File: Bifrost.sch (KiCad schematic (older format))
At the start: 28 parts, among them IC1 DS1085Z-10+, IC2 DS1085Z-10+, J1 OIP, J10 Barrel_Jack_Switch, J5 CalCK

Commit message: Added soldering options
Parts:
- added R10, R13, R14, R17, R18, R19, R3, R4, R5, R6, R9: 0, Resistor_SMD:R_0603_1608Metric_Pad0.98x0.95mm_HandSolder, symbol Device:R
- gave numbers to parts that had none: 4
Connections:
- wire segments 118 -> 145
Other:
- moved on the sheet: IC1, IC2, IOH1, J1, J10, J5, R1, R2, R49, R52, R53, R56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

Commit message: Added Logic gate buffer for the oscillator
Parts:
- removed U3, U4: BPF-E16, LibPersoNadj:Mini-Circuits_HR1176, symbol LibPersoNadj:BPF-E16
- added U5, U6: 74AHC1G04, Package_TO_SOT_SMD:SOT-353_SC-70-5, symbol 74xGxx:74AHC1G04
- RV1, RV2: footprint (none) -> Potentiometer_THT:Potentiometer_Bourns_3266Y_Vertical
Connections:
- net labels added: VDD
- wire segments 145 -> 147
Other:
- moved on the sheet: IC1, IC2, POWER1, R100, R71, R72

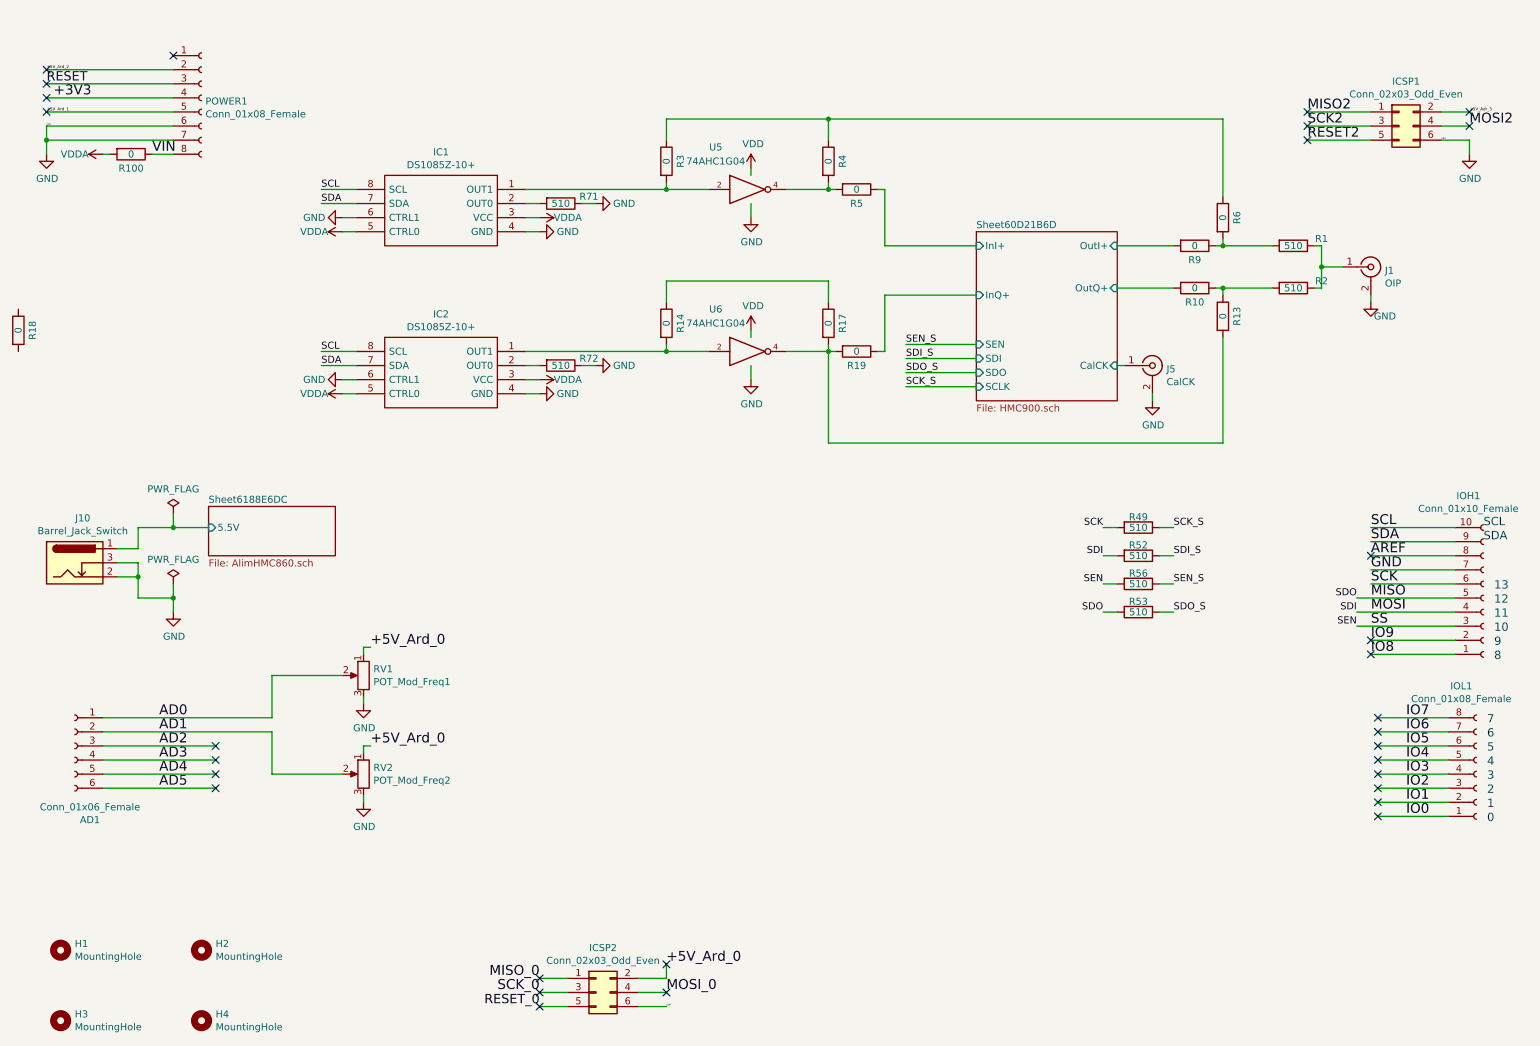
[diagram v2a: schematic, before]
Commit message: Added filtering capa and rearanged analogue in (A1=>A4)
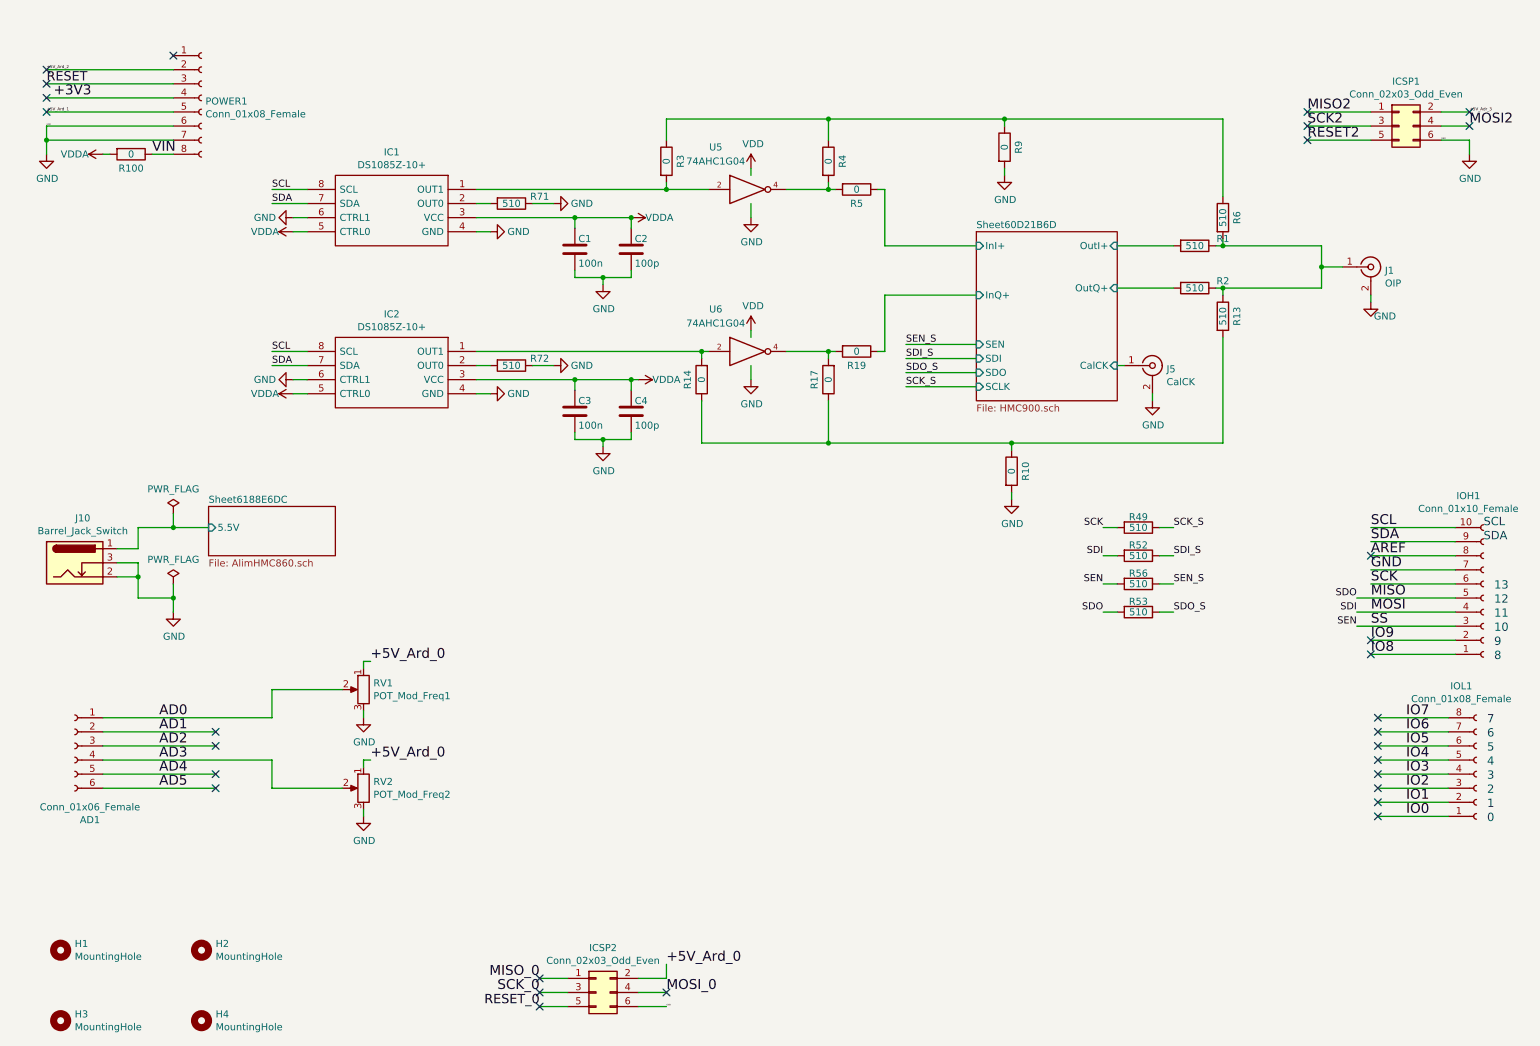
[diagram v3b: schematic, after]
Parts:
- removed R18: 0, Resistor_SMD:R_0603_1608Metric_Pad0.98x0.95mm_HandSolder, symbol Device:R
- added C1, C3: 100n, Capacitor_SMD:C_0603_1608Metric_Pad1.08x0.95mm_HandSolder, symbol Device:C
- added C2, C4: 100p, Capacitor_SMD:C_0603_1608Metric_Pad1.08x0.95mm_HandSolder, symbol Device:C
- R13, R6: value 0 -> 510
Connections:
- net AD1: no longer RV2.2
- net AD3: now also RV2.2
- net GND: now also R10.2, R9.2, C1.1, C2.1, C3.1, C4.1
- net Sheet60D21B6D/OutI+: now also R1.2; no longer R9.2
- net Sheet60D21B6D/OutQ+: now also R2.2; no longer R10.2
- net VDDA: now also C1.2, C2.2, C3.2, C4.2
- net at J1.1 (In), R1.1, R2.1: now also R13.1, R6.2
- net at R17.2, R19.2, U6.4: no longer R13.2
- net at R3.1, R4.1, R6.1: now also R9.1
- net at R14.1, R17.1: now also R10.1, R13.2
- no-connect marks 30 -> 29
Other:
- moved on the sheet: IC1, IC2, R1, R14, R17, R2, R71, R72, RV1, RV2

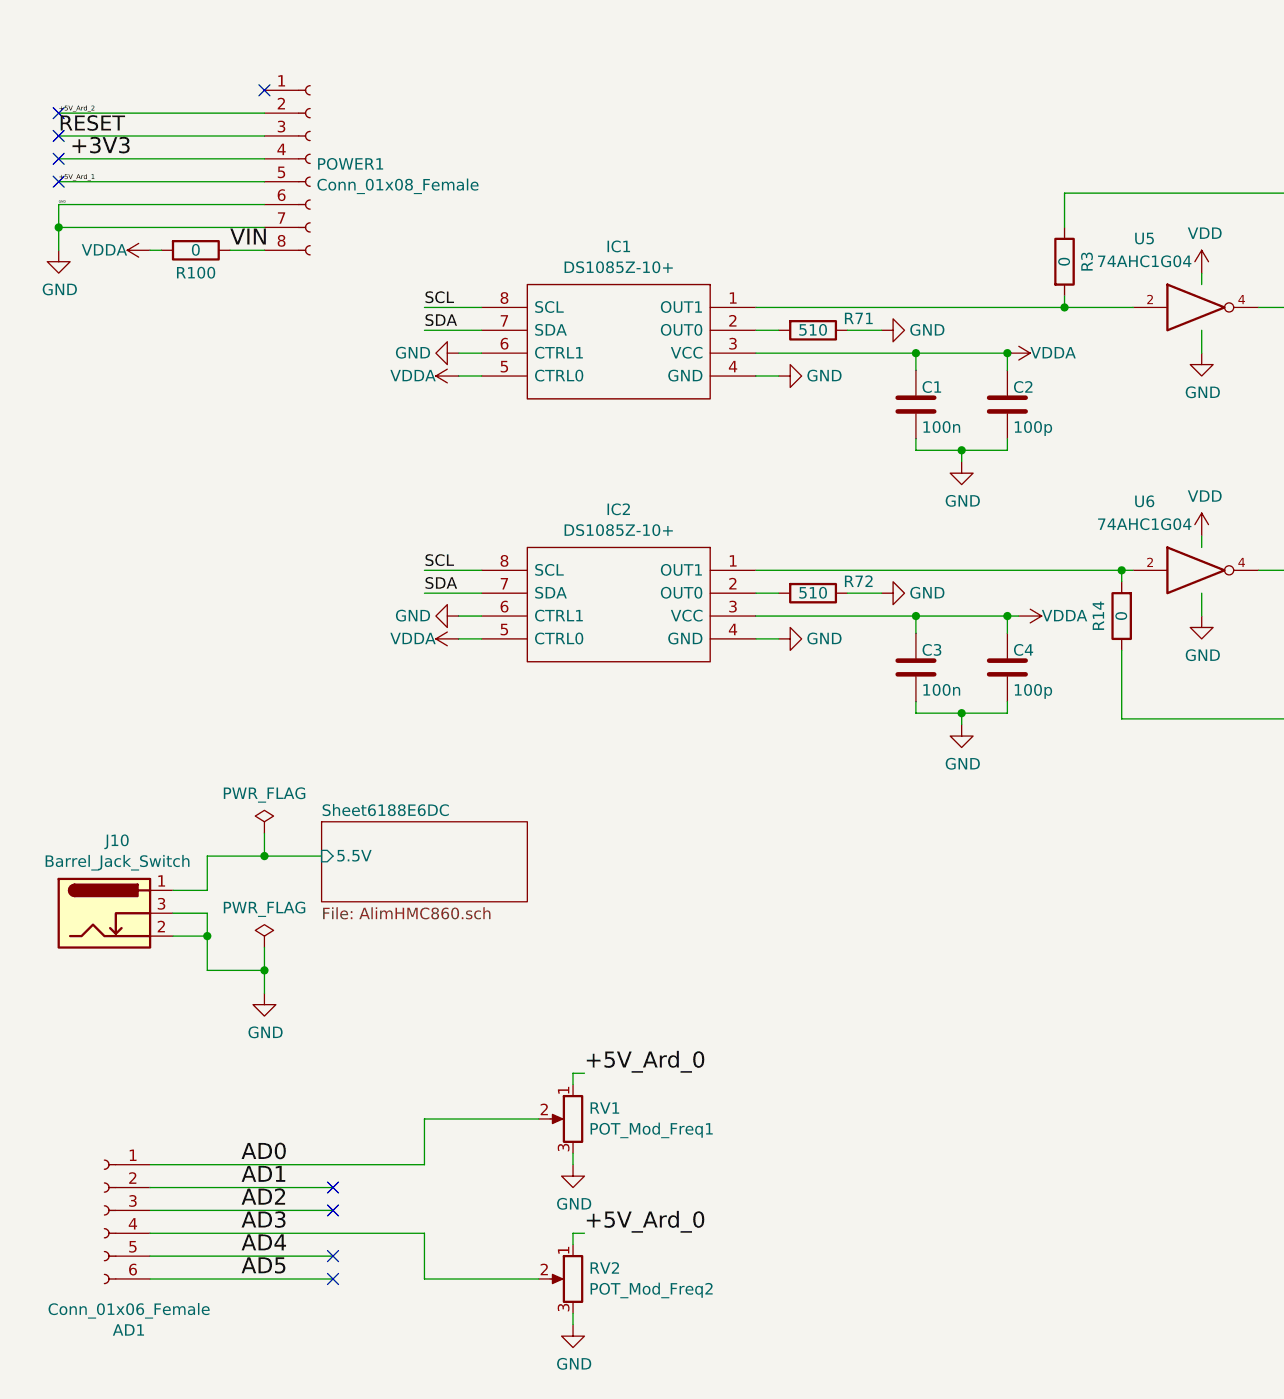
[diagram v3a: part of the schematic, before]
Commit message: added cavalier on the oscillator's power
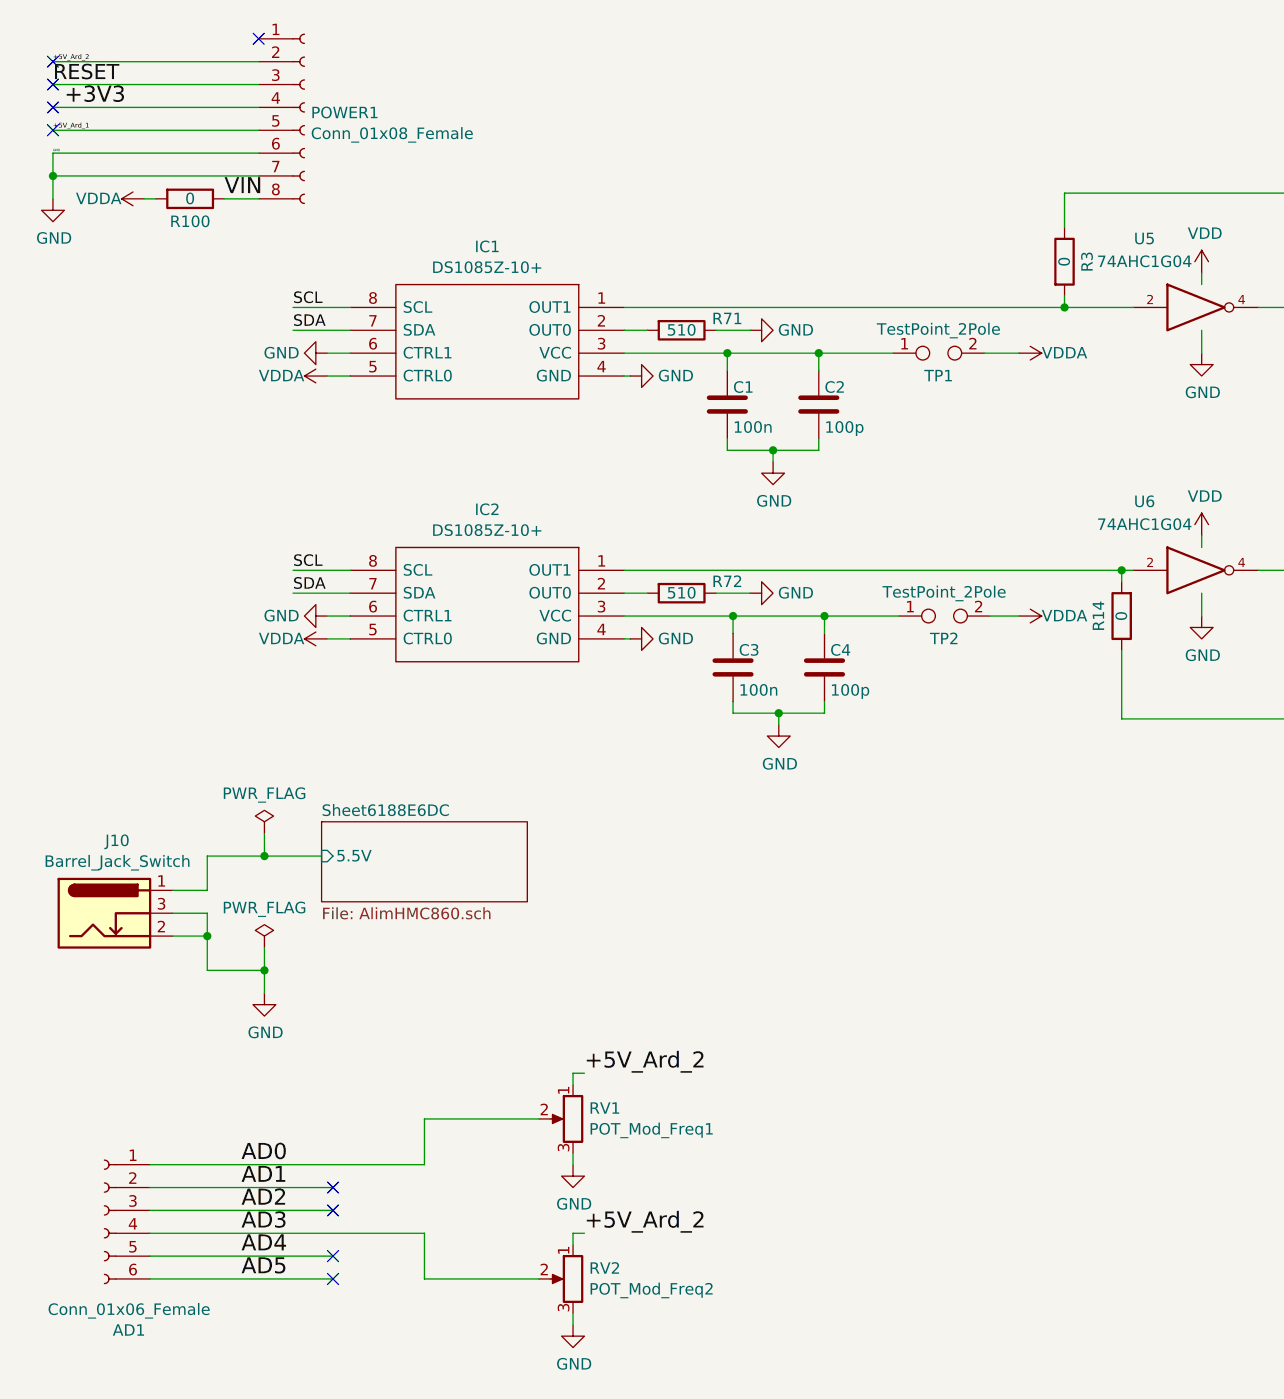
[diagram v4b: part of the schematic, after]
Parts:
- added TP1, TP2: TestPoint_2Pole, Connector_PinHeader_2.54mm:PinHeader_1x02_P2.54mm_Vertical, symbol Connector:TestPoint_2Pole
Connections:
- net +5V_Ard_0: no longer RV1.1, RV2.1
- net +5V_Ard_2: now also RV1.1, RV2.1
- net VDDA: now also TP1.2, TP2.2; no longer C1.2, C2.2, C3.2, C4.2, IC1.3 (VCC), IC2.3 (VCC)
- new net: C1.2, C2.2, IC1.3 (VCC), TP1.1
- new net: C3.2, C4.2, IC2.3 (VCC), TP2.1
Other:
- moved on the sheet: C1, C2, C3, C4, IC1, IC2, POWER1, R100, R71, R72

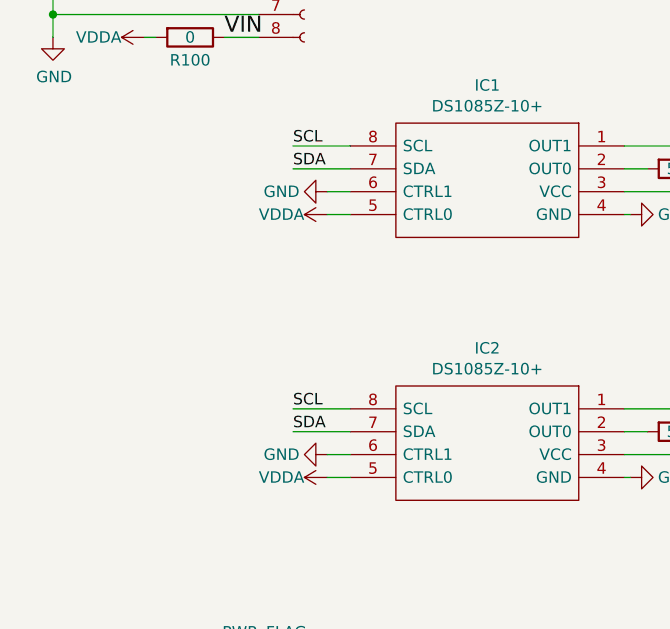
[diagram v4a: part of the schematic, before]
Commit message: Connected the oscillators enable to the arduino
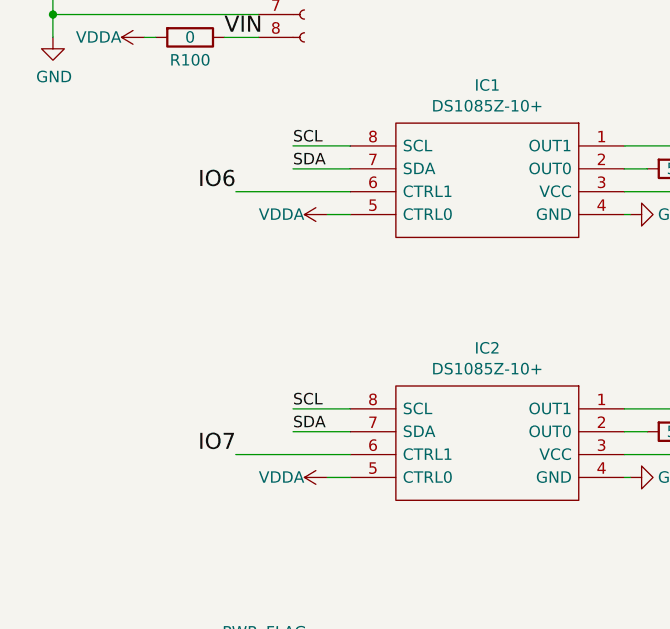
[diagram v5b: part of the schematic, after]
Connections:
- net GND: no longer IC1.6 (CTRL1), IC2.6 (CTRL1)
- net IO6: now also IC1.6 (CTRL1)
- net IO7: now also IC2.6 (CTRL1)
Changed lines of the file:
@@
-	0    1    1    0
-$EndComp
-Wire Wire Line
-	1775 2050 1875 2050
-$Comp
-L power:VDDA #PWR0111
-U 1 1 60E66581
-P 1775 2050
-F 0 "#PWR0111" H 1775 1900 50  0001 C CNN
-F 1 "VDDA" V 1775 2250 50  0000 C CNN
-F 2 "" H 1775 2050 50  0001 C CNN
-F 3 "" H 1775 2050 50  0001 C CNN
-	1    1775 2050
-	0    -1   -1   0
-$EndComp
-Wire Wire Line
-	1875 1950 1775 1950
-$Comp
-L power:GND #PWR?
-U 1 1 60E620C9
-P 1775 1950
-AR Path="/60D21B6E/60E620C9" Ref="#PWR?"  Part="1"
-AR Path="/60E620C9" Ref="#PWR0110"  Part="1"
-F 0 "#PWR0110" H 1775 1700 50  0001 C CNN
-F 1 "GND" V 1775 1750 50  0000 C CNN
-F 2 "" H 1775 1950 50  0001 C CNN
-F 3 "" H 1775 1950 50  0001 C CNN
-	1    1775 1950
 	0    1    1    0
 $EndComp
@@
 SCL
 $Comp
-L power:GND #PWR?
-U 1 1 60E6CC1E
-P 1775 3100
-AR Path="/60D21B6E/60E6CC1E" Ref="#PWR?"  Part="1"
-AR Path="/60E6CC1E" Ref="#PWR0112"  Part="1"
-F 0 "#PWR0112" H 1775 2850 50  0001 C CNN
-F 1 "GND" V 1775 2900 50  0000 C CNN
-F 2 "" H 1775 3100 50  0001 C CNN
-F 3 "" H 1775 3100 50  0001 C CNN
-	1    1775 3100
-	0    1    1    0
-$EndComp
-Wire Wire Line
-	1875 3100 1775 3100
-$Comp
-L power:VDDA #PWR0113
-U 1 1 60E6CC29
-P 1775 3200
-F 0 "#PWR0113" H 1775 3050 50  0001 C CNN
-F 1 "VDDA" V 1775 3400 50  0000 C CNN
-F 2 "" H 1775 3200 50  0001 C CNN
-F 3 "" H 1775 3200 50  0001 C CNN
-	1    1775 3200
-	0    -1   -1   0
-$EndComp
-Wire Wire Line
-	1775 3200 1875 3200
-$Comp
 L Device:R R72
 U 1 1 60E9F752
@@
 Wire Wire Line
 	4675 3100 4800 3100
+Text Label 1375 1950 2    70   ~ 0
+IO6
+Wire Wire Line
+	1375 1950 1875 1950
+Wire Wire Line
+	1775 3200 1875 3200
+$Comp
+L power:VDDA #PWR0113
+U 1 1 60E6CC29
+P 1775 3200
+F 0 "#PWR0113" H 1775 3050 50  0001 C CNN
+F 1 "VDDA" V 1775 3400 50  0000 C CNN
+F 2 "" H 1775 3200 50  0001 C CNN
+F 3 "" H 1775 3200 50  0001 C CNN
+	1    1775 3200
+	0    -1   -1   0
+$EndComp
+Wire Wire Line
+	1375 3100 1875 3100
+Text Label 1375 3100 2    70   ~ 0
+IO7
+Wire Wire Line
+	1775 2050 1875 2050
+$Comp
+L power:VDDA #PWR?
+U 1 1 610ED303
+P 1775 2050
+F 0 "#PWR?" H 1775 1900 50  0001 C CNN
+F 1 "VDDA" V 1775 2250 50  0000 C CNN
+F 2 "" H 1775 2050 50  0001 C CNN
+F 3 "" H 1775 2050 50  0001 C CNN
+	1    1775 2050
+	0    -1   -1   0
+$EndComp
 $EndSCHEMATC
